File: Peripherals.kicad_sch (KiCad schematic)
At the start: 23 parts, among them J3 1040310811, U5 LSM6DSV, U8 SN74AXC4T774RSVR

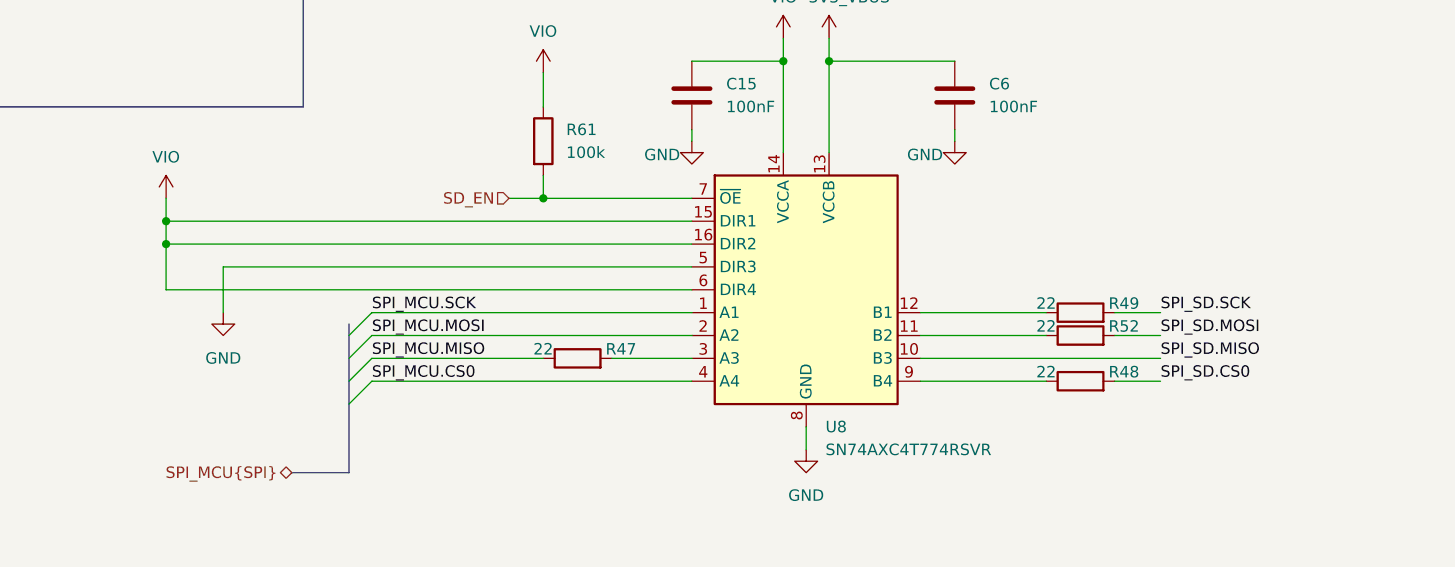
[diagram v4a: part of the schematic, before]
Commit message: Add comments from layout meeting 20.07.2026
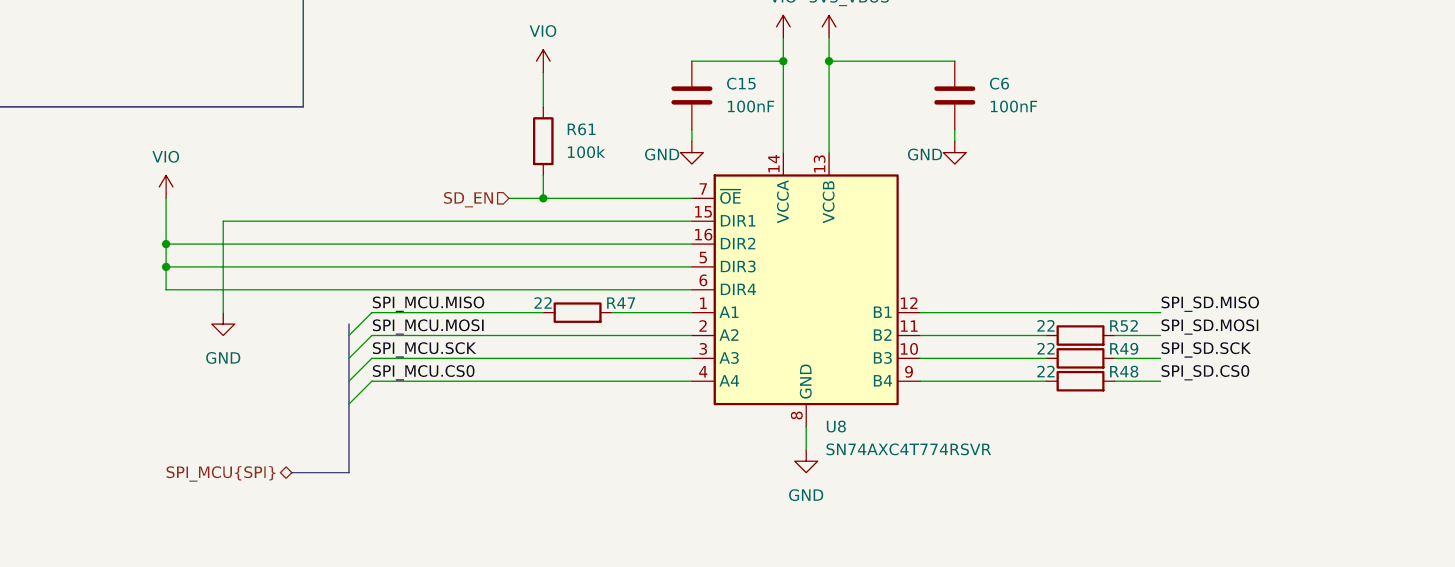
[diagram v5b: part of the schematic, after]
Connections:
- net GND: now also U8.15 (DIR1); no longer U8.5 (DIR3)
- net SPI_MCU.SCK: now also U8.3 (A3); no longer U8.1 (A1)
- net SPI_SD.MISO: now also U8.12 (B1); no longer U8.10 (B3)
- net VIO: now also U8.5 (DIR3); no longer U8.15 (DIR1)
- net at R49.1: now also U8.10 (B3); no longer U8.12 (B1)
- net at R47.2: now also U8.1 (A1); no longer U8.3 (A3)
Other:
- moved on the sheet: R47, R49
